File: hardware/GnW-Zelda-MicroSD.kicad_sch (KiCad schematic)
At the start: 7 parts, among them J1 Castellated_Edge_7P, J2 Battery_Tap_2P, J3 MicroSD_Socket_TFP09, U2 RT9193-28GB

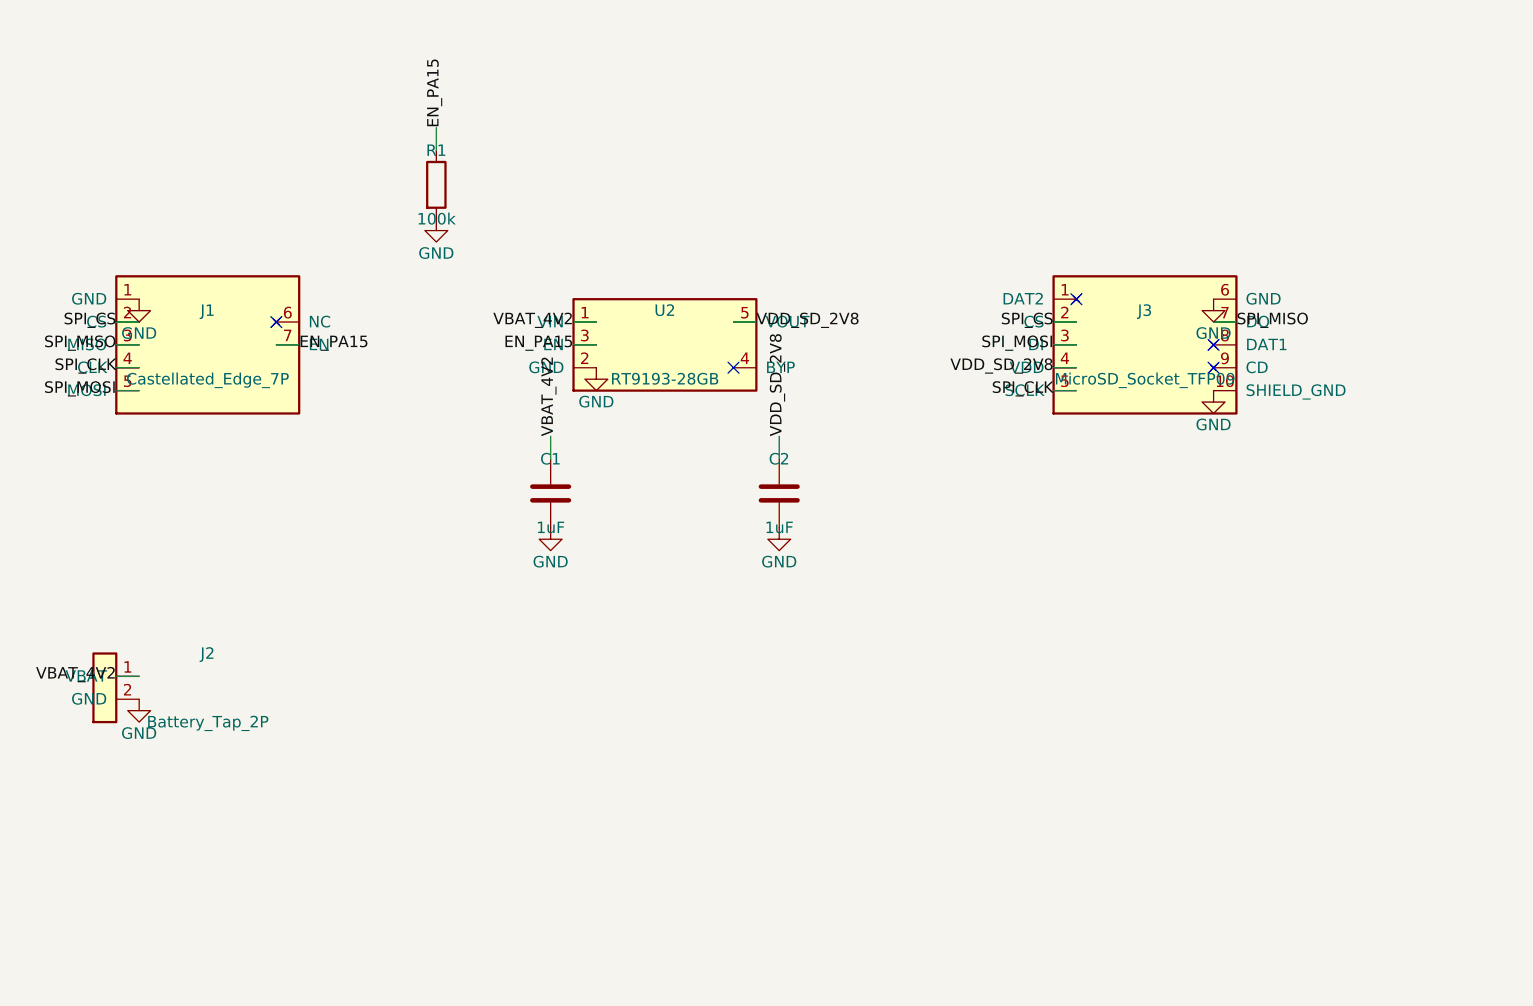
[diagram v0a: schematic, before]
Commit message: Swap J2/J3/U1 to PrimoAngelo's real footprints, fix ref-designator and net-naming bugs
J2 (microSD socket) and J3 (VBAT tab) now use real MSD1A/Pad_1x1_5
geometry from PrimoAngelo's native KiCad library instead of RE'd
approximations; U1 gets a real RT9193 STEP model. C1/C2/R1 get a second,
real hand-solder-0805 footprint stacked at their original location for
package-size flexibility.

Also fixes: schematic/PCB reference-designator swap (J2/J3, U1/U2), a
batch of inconsistent net names left over from re-syncing the PCB from
schematic (local net labels converted to global to prevent recurrence),
and 8 undersized vias failing min-hole-size DRC.
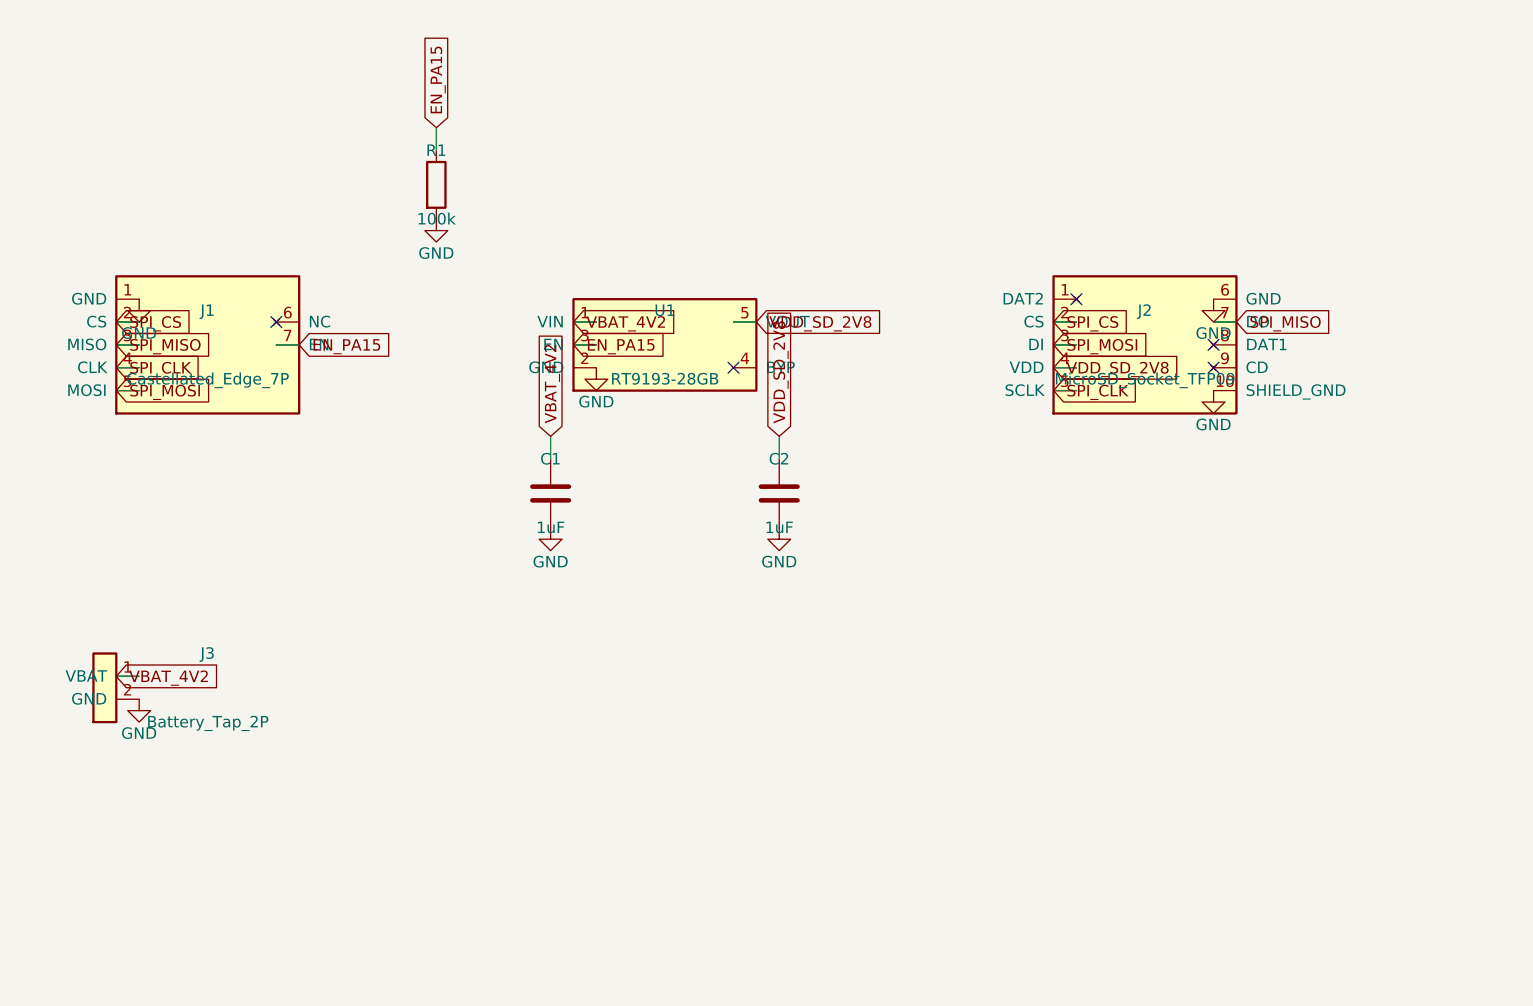
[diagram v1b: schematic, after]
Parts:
- J2: renamed from J3; footprint Connector_Card:microSD_HC_Molex_104031-0811 -> PrimoAngelo_FG_MicroSD:MSD1A
- J3: renamed from J2; footprint (none) -> PrimoAngelo_Pad:Pad_1x1_5
- U1: renamed from U2; footprint Package_TO_SOT_SMD:SOT-23-5 -> RT9193_exact

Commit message: Clean up schematic layout and silkscreen
Manual schematic relayout (wires/symbols, no connectivity changes --
component roster and net topology unchanged, verified via ERC/DRC). PCB
silkscreen cleanup: R1/C1/C2 values moved from F.Fab to F.SilkS so
they're visible on the physical board, U1's reference text replaced with
its part number (RT9193-28GB) since it's the board's only IC and "U1"
isn't descriptive, and a "4V" label added near the VBAT tap (J3).
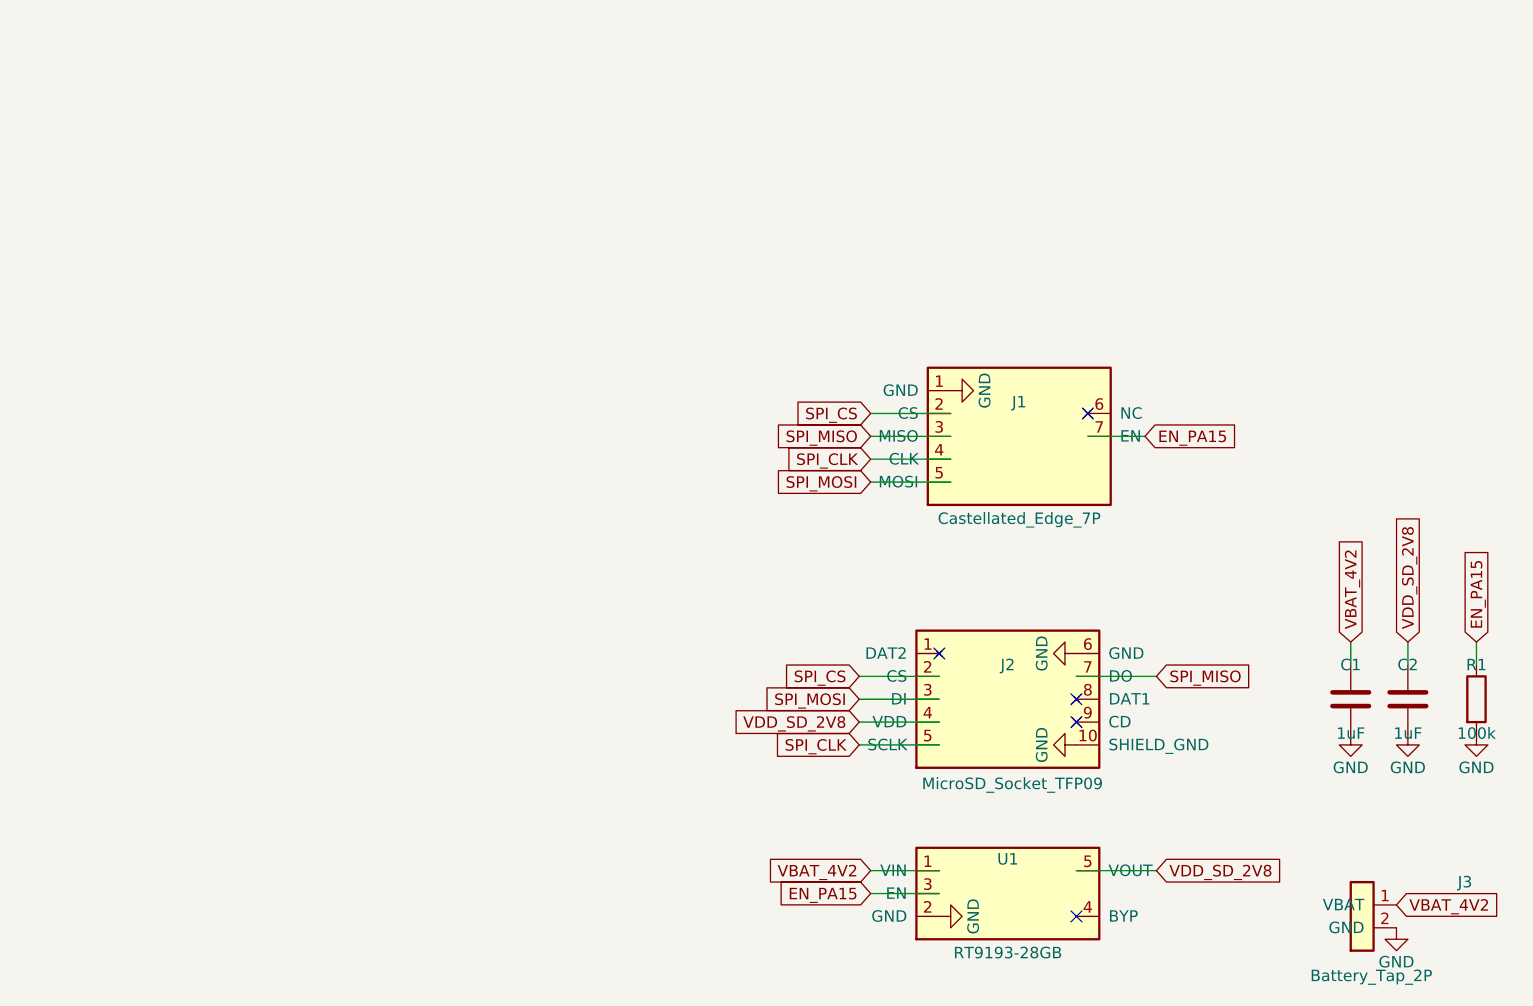
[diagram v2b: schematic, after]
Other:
- moved on the sheet: C1, C2, J1, J2, J3, R1, U1
